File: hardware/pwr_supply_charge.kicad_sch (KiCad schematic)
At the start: 34 parts, among them J1 Battery Input, J2 Power Switch, J3 USB_C_Receptacle_USB2.0_14P, Q1 CSD17581Q3A, Q2 CSD17581Q3A, Q3 AO4435, Q4 AO4468, U1 HY2120, U2 INA226, U3 CN3302

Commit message: rm cached
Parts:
- U2: footprint Package_SO:VSSOP-10_3x3mm_P0.5mm -> Package_SO:TSSOP-10_3x3mm_P0.5mm

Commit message: First routing draft
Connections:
- net B+: now also J2.2 (Pin_2); no longer J2.1 (Pin_1)
- net V_BATT: now also J2.1 (Pin_1); no longer J2.2 (Pin_2)
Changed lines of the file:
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@@
 	)
 	(junction
-		(at 50.8 57.15)
-		(diameter 0)
-		(color 0 0 0 0)
-	)
-	(junction
 		(at 96.52 138.43)
 		(diameter 0)
@@
 	)
 	(junction
+		(at 50.8 54.61)
+		(diameter 0)
+		(color 0 0 0 0)
+	)
+	(junction
 		(at 76.2 138.43)
 		(diameter 0)
@@
 	(wire
 		(pts
-			(xy 50.8 57.15) (xy 59.69 57.15)
-		)
-		(stroke
-			(width 0.381)
-			(type default)
-		)
-	)
-	(wire
-		(pts
 			(xy 45.72 36.83) (xy 50.8 36.83)
 		)
@@
 	(wire
 		(pts
-			(xy 45.72 54.61) (xy 59.69 54.61)
+			(xy 45.72 54.61) (xy 50.8 54.61)
 		)
 		(stroke
@@
 	(wire
 		(pts
+			(xy 50.8 54.61) (xy 59.69 54.61)
+		)
+		(stroke
+			(width 0.381)
+			(type default)
+		)
+	)
+	(wire
+		(pts
 			(xy 238.76 128.27) (xy 238.76 97.79)
 		)
@@
 	(wire
 		(pts
-			(xy 45.72 57.15) (xy 50.8 57.15)
+			(xy 45.72 57.15) (xy 59.69 57.15)
 		)
 		(stroke
@@
 		)
 	)
+	(label "V_BATT"
+		(at 45.72 54.61 180)
+		(effects
+			(font
+				(size 1.27 1.27)
+			)
+			(justify right bottom)
+		)
+	)
 	(label "B-"
 		(at 45.72 39.37 180)
@@
 	)
 	(label "B+"
-		(at 45.72 54.61 180)
+		(at 45.72 57.15 180)
 		(effects
 			(font
@@
 	)
 	(label "V_BATT"
-		(at 45.72 57.15 180)
-		(effects
-			(font
-				(size 1.27 1.27)
-			)
-			(justify right bottom)
-		)
-	)
-	(label "V_BATT"
 		(at 201.93 43.18 180)
 		(effects
@@
 	)
 	(symbol
+		(lib_id "power:PWR_FLAG")
+		(at 50.8 54.61 0)
+		(unit 1)
+		(body_style 1)
+		(exclude_from_sim no)
+		(in_bom yes)
+		(on_board yes)
+		(in_pos_files yes)
+		(dnp no)
+		(fields_autoplaced yes)
+		(property "Reference" "#FLG06"
+			(at 50.8 52.705 0)
+			(hide yes)
+			(show_name no)
+			(do_not_autoplace no)
+			(effects
+				(font
+					(size 1.27 1.27)
+				)
+			)
+		)
+		(property "Value" "PWR_FLAG"
+			(at 50.8 49.53 0)
+			(show_name no)
+			(do_not_autoplace no)
+			(effects
+				(font
+					(size 1.27 1.27)
+				)
+			)
+		)
+		(property "Footprint" ""
+			(at 50.8 54.61 0)
+			(hide yes)
+			(show_name no)
+			(do_not_autoplace no)
+			(effects
+				(font
+					(size 1.27 1.27)
+				)
+			)
+		)
+		(property "Datasheet" ""
+			(at 50.8 54.61 0)
+			(hide yes)
+			(show_name no)
+			(do_not_autoplace no)
+			(effects
+				(font
+					(size 1.27 1.27)
+				)
+			)
+		)
+		(property "Description" "Special symbol for telling ERC where power comes from"
+			(at 50.8 54.61 0)
+			(hide yes)
+			(show_name no)
+			(do_not_autoplace no)
+			(effects
+				(font
+					(size 1.27 1.27)
+				)
+			)
+		)
+		(pin "1"
+		)
+		(instances
+			(project "chromapi_motherboard_v1"
+				(path "/d1a31f26-03e0-43e1-89c1-031fe31befc5/2dc5047f-e6b9-4c1e-8ac3-300835122eb4"
+					(reference "#FLG06")
+					(unit 1)
+				)
+			)
+		)
+	)
+	(symbol
 		(lib_id "Connector_Generic:Conn_01x02")
 		(at 64.77 54.61 0)
@@
 					(unit 1)
 				)
-			)
-		)
-	)
-	(symbol
-		(lib_id "power:PWR_FLAG")
-		(at 50.8 57.15 180)
-		(unit 1)
-		(body_style 1)
-		(exclude_from_sim no)
-		(in_bom yes)
-		(on_board yes)
-		(in_pos_files yes)
-		(dnp no)
-		(fields_autoplaced yes)
-		(property "Reference" "#FLG06"
-			(at 50.8 59.055 0)
-			(hide yes)
-			(show_name no)
-			(do_not_autoplace no)
-			(effects
-				(font
-					(size 1.27 1.27)
-				)
-			)
-		)
-		(property "Value" "PWR_FLAG"
-			(at 50.8 62.23 0)
-			(show_name no)
-			(do_not_autoplace no)
-			(effects
-				(font
-					(size 1.27 1.27)
-				)
-			)
-		)
-		(property "Footprint" ""
-			(at 50.8 57.15 0)
-			(hide yes)
-			(show_name no)
-			(do_not_autoplace no)
-			(effects
-				(font
-					(size 1.27 1.27)
-				)
-			)
-		)
-		(property "Datasheet" ""
-			(at 50.8 57.15 0)
-			(hide yes)
-			(show_name no)
-			(do_not_autoplace no)
-			(effects
-				(font
-					(size 1.27 1.27)
-				)
-			)
-		)
-		(property "Description" "Special symbol for telling ERC where power comes from"
-			(at 50.8 57.15 0)
-			(hide yes)
-			(show_name no)
-			(do_not_autoplace no)
-			(effects
-				(font
-					(size 1.27 1.27)
-				)
-			)
-		)
-		(pin "1"
-		)
-		(instances
-			(project "chromapi_motherboard_v1"
-				(path "/d1a31f26-03e0-43e1-89c1-031fe31befc5/2dc5047f-e6b9-4c1e-8ac3-300835122eb4"
-					(reference "#FLG06")
-					(unit 1)
-				)

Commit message: Routing update
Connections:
- net B-: now also J1.2 (Pin_2); no longer J1.3 (Pin_3)
- net BM: now also J1.3 (Pin_3); no longer J1.2 (Pin_2)
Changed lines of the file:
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@@
 		)
 	)
-	(label "V_BATT"
-		(at 45.72 54.61 180)
+	(label "B-"
+		(at 45.72 36.83 180)
 		(effects
 			(font
@@
 		)
 	)
-	(label "B-"
-		(at 45.72 39.37 180)
-		(effects
-			(font
-				(size 1.27 1.27)
-			)
-			(justify right bottom)
-		)
-	)
-	(label "BM"
-		(at 45.72 36.83 180)
+	(label "V_BATT"
+		(at 45.72 54.61 180)
 		(effects
 			(font
@@
 		(effects
 			(font
+				(size 1.27 1.27)
+			)
+			(justify right bottom)
+		)
+	)
+	(label "BM"
+		(at 45.72 39.37 180)
+		(effects
+			(font

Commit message: minor fix
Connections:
- net GND: now also J3.SH (SHIELD); no longer J3.S1 (SHIELD)
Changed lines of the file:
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@@
 	)
 	(symbol
+		(lib_id "Connector:USB_C_Receptacle_USB2.0_14P")
+		(at 76.2 113.03 0)
+		(unit 1)
+		(body_style 1)
+		(exclude_from_sim no)
+		(in_bom yes)
+		(on_board yes)
+		(in_pos_files yes)
+		(dnp no)
+		(fields_autoplaced yes)
+		(property "Reference" "J3"
+			(at 76.2 90.17 0)
+			(show_name no)
+			(do_not_autoplace no)
+			(effects
+				(font
+					(size 1.27 1.27)
+				)
+			)
+		)
+		(property "Value" "USB_C_Receptacle_USB2.0_14P"
+			(at 76.2 92.71 0)
+			(show_name no)
+			(do_not_autoplace no)
+			(effects
+				(font
+					(size 1.27 1.27)
+				)
+			)
+		)
+		(property "Footprint" "Connector_USB:USB_C_Receptacle_HRO_TYPE-C-31-M-12"
+			(at 80.01 113.03 0)
+			(hide yes)
+			(show_name no)
+			(do_not_autoplace no)
+			(effects
+				(font
+					(size 1.27 1.27)
+				)
+			)
+		)
+		(property "Datasheet" "https://www.usb.org/sites/default/files/documents/usb_type-c.zip"
+			(at 80.01 113.03 0)
+			(hide yes)
+			(show_name no)
+			(do_not_autoplace no)
+			(effects
+				(font
+					(size 1.27 1.27)
+				)
+			)
+		)
+		(property "Description" "USB 2.0-only 14P Type-C Receptacle connector"
+			(at 76.2 113.03 0)
+			(hide yes)
+			(show_name no)
+			(do_not_autoplace no)
+			(effects
+				(font
+					(size 1.27 1.27)
+				)
+			)
+		)
+		(pin "B1"
+		)
+		(pin "A1"
+		)
+		(pin "A7"
+		)
+		(pin "A5"
+		)
+		(pin "A6"
+		)
+		(pin "A9"
+		)
+		(pin "A12"
+		)
+		(pin "A4"
+		)
+		(pin "B5"
+		)
+		(pin "B7"
+		)
+		(pin "B9"
+		)
+		(pin "B4"
+		)
+		(pin "B12"
+		)
+		(pin "B6"
+		)
+		(pin "SH"
+		)
+		(instances
+			(project "chromapi_motherboard_v1"
+				(path "/d1a31f26-03e0-43e1-89c1-031fe31befc5/2dc5047f-e6b9-4c1e-8ac3-300835122eb4"
+					(reference "J3")
+					(unit 1)
+				)
+			)
+		)
+	)
+	(symbol
 		(lib_id "hy2120:HY2120")
 		(at 158.75 43.18 0)
@@
 					(unit 1)
 				)
-			)
-		)
-	)
-	(symbol
-		(lib_id "Connector:USB_C_Receptacle_USB2.0_14P")
-		(at 76.2 113.03 0)
-		(unit 1)
-		(body_style 1)
-		(exclude_from_sim no)
-		(in_bom yes)
-		(on_board yes)
-		(in_pos_files yes)
-		(dnp no)
-		(fields_autoplaced yes)
-		(property "Reference" "J3"
-			(at 76.2 90.17 0)
-			(show_name no)
-			(do_not_autoplace no)
-			(effects
-				(font
-					(size 1.27 1.27)
-				)
-			)
-		)
-		(property "Value" "USB_C_Receptacle_USB2.0_14P"
-			(at 76.2 92.71 0)
-			(show_name no)
-			(do_not_autoplace no)
-			(effects
-				(font
-					(size 1.27 1.27)
-				)
-			)
-		)
-		(property "Footprint" "Connector_USB:USB_C_Receptacle_HRO_TYPE-C-31-M-12"
-			(at 80.01 113.03 0)
-			(hide yes)
-			(show_name no)
-			(do_not_autoplace no)
-			(effects
-				(font
-					(size 1.27 1.27)
-				)
-			)
-		)
-		(property "Datasheet" "https://github.com/Mowibox/chromapi_motherboard/blob/main/docs/datasheets/usb_type-c.zip"
-			(at 80.01 113.03 0)
-			(hide yes)
-			(show_name no)
-			(do_not_autoplace no)
-			(effects
-				(font
-					(size 1.27 1.27)
-				)
-			)
-		)
-		(property "Description" "USB 2.0-only 14P Type-C Receptacle connector"
-			(at 76.2 113.03 0)
-			(hide yes)
-			(show_name no)
-			(do_not_autoplace no)
-			(effects
-				(font
-					(size 1.27 1.27)
-				)
-			)
-		)
-		(property "Sim.Device" ""
-			(at 76.2 113.03 0)
-			(hide yes)
-			(show_name no)
-			(do_not_autoplace no)
-			(effects
-				(font
-					(size 1.27 1.27)
-				)
-			)
-		)
-		(property "Sim.Type" ""
-			(at 76.2 113.03 0)
-			(hide yes)
-			(show_name no)
-			(do_not_autoplace no)
-			(effects
-				(font
-					(size 1.27 1.27)
-				)
-			)
-		)
-		(property "Author" ""
-			(at 76.2 113.03 0)
-			(hide yes)
-			(show_name no)
-			(do_not_autoplace no)
-			(effects
-				(font
-					(size 1.27 1.27)
-				)
-			)
-		)
-		(property "License" ""
-			(at 76.2 113.03 0)
-			(hide yes)
-			(show_name no)
-			(do_not_autoplace no)
-			(effects
-				(font
-					(size 1.27 1.27)
-				)
-			)
-		)
-		(property "Manufacturer" ""
-			(at 76.2 113.03 0)
-			(hide yes)
-			(show_name no)
-			(do_not_autoplace no)
-			(effects
-				(font
-					(size 1.27 1.27)
-				)
-			)
-		)
-		(pin "A4"
-		)
-		(pin "A12"
-		)
-		(pin "A1"
-		)
-		(pin "A5"
-		)
-		(pin "B9"
-		)
-		(pin "A6"
-		)
-		(pin "B1"
-		)
-		(pin "B6"
-		)
-		(pin "B7"
-		)
-		(pin "A9"
-		)
-		(pin "B4"
-		)
-		(pin "S1"
-		)
-		(pin "A7"
-		)
-		(pin "B5"
-		)
-		(pin "B12"
-		)
-		(instances
-			(project "chromapi_motherboard_v1"
-				(path "/d1a31f26-03e0-43e1-89c1-031fe31befc5/2dc5047f-e6b9-4c1e-8ac3-300835122eb4"
-					(reference "J3")
-					(unit 1)
-				)

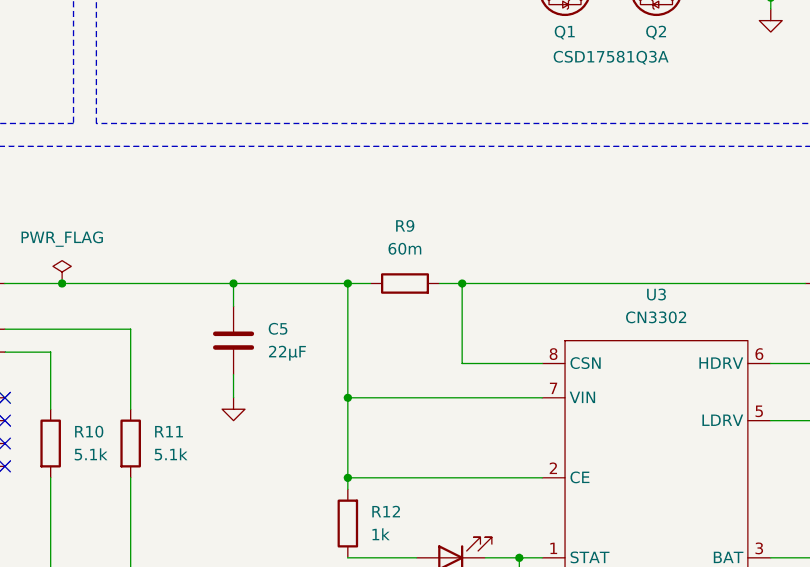
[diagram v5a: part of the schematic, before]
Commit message: Rerouting USB charge
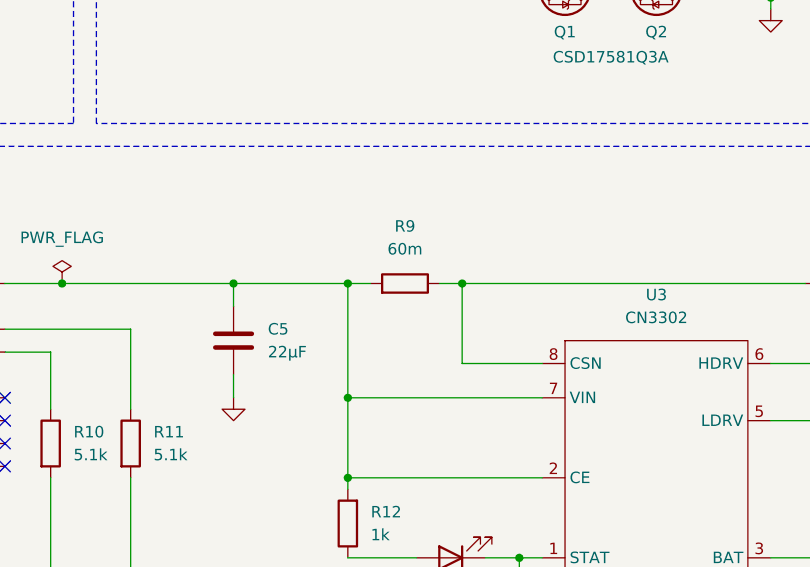
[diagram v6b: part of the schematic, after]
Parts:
- R9: footprint Resistor_SMD:R_0603_1608Metric -> Resistor_SMD:R_1206_3216Metric
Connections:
- net at C5.1, J3.A4 (VBUS), J3.A9 (VBUS)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: now also R9.2; no longer R9.1
- net at Q3.1, Q3.2, Q3.3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: now also R9.1; no longer R9.2
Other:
- moved on the sheet: R9
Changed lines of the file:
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@@
 	(symbol
 		(lib_id "Device:R")
-		(at 135.89 97.79 90)
+		(at 135.89 97.79 270)
+		(mirror x)
 		(unit 1)
 		(body_style 1)
@@
 		(in_pos_files yes)
 		(dnp no)
-		(fields_autoplaced yes)
 		(property "Reference" "R9"
 			(at 135.89 91.44 90)
@@
 			)
 		)
-		(property "Footprint" "Resistor_SMD:R_0603_1608Metric"
+		(property "Footprint" "Resistor_SMD:R_1206_3216Metric"
 			(at 135.89 99.568 90)
 			(hide yes)

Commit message: Updating MPN and part number
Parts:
- D1, D2: JLCPCB Part# (none) -> C8678; MPN (none) -> SS34
- Q1, Q2: JLCPCB Part# (none) -> C2861705; MPN (none) -> CSD17581Q3A
- Q3: JLCPCB Part# (none) -> C79714
- Q4: JLCPCB Part# (none) -> C87410; MPN (none) -> AO4468
- U1: JLCPCB Part# (none) -> C116509; MPN (none) -> HY2120-CB
- U2: JLCPCB Part# (none) -> C2653835; MPN (none) -> INA226AQDGSRQ1
- U3: JLCPCB Part# (none) -> C559039; MPN (none) -> CN3302

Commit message: Updating BOM
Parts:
- C1, C4: JLCPCB Part# (none) -> C1591; MPN (none) -> CL10B104KB8NNNC
- C2, C3: JLCPCB Part# (none) -> C307331; MPN (none) -> CL05B104KB54PNC
- C5, C6: value 22µF -> 22uF; symbol Device:C -> Device:C_Polarized
- L1: value 4.7µH -> 4.7uH
